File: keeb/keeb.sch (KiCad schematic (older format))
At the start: 156 parts, among them J1 AudioJack3, J101 USB_C_Receptacle_USB2.0, J102 AVR-ISP-6, SW101 SW_Push, SW102 SW_Push, SW103 SW_Push, SW104 SW_Push, SW105 SW_Push, SW106 SW_Push, SW107 SW_Push, SW108 SW_Push, SW109 SW_Push, SW110 SW_Push, SW111 SW_Push, SW112 SW_Push, SW113 SW_Push, SW114 SW_Push, SW115 SW_Push, SW116 SW_Push, SW117 SW_Push, SW118 SW_Push, SW119 SW_Push, SW120 SW_Push, SW121 SW_Push, SW122 SW_Push, SW123 SW_Push, SW124 SW_Push, SW125 SW_Push, SW126 SW_Push, SW127 SW_Push, SW128 SW_Push, SW129 SW_Push, SW130 SW_Push, SW131 SW_Push, SW132 SW_Push, SW133 SW_Push, SW134 SW_Push, SW135 SW_Push, SW136 SW_Push, SW137 SW_Push, SW138 SW_Push, SW139 SW_Push, SW140 SW_Push, SW141 SW_Push, SW142 SW_Push, SW143 SW_Push, SW144 SW_Push, SW145 SW_Push, SW146 SW_Push, SW147 SW_Push, SW148 SW_Push, SW149 SW_Push, SW150 SW_Push, SW151 SW_Push, SW152 SW_Push, SW153 SW_Push, SW154 SW_Push, SW155 SW_Push, SW156 SW_Push, SW157 SW_Push, SW158 SW_Push, SW159 SW_Push, SW160 SW_Push, SW161 SW_Push, SW162 SW_Push, SW163 SW_Push, SW164 SW_Push, SW165 SW_Push, SW166 SW_Push, SW167 SW_Push, U102 ATmega32U4-AU, Y1 16Mhz

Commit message: i2c fin
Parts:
- removed J1: AudioJack3, Connector_Audio:Jack_3.5mm_CUI_SJ-3523-SMT_Horizontal, symbol Connector:AudioJack3
- added J103, J104: AudioJack4, unORTHOdox_CF:Jack_3.5mm_TIC54-00177_Horizontal, symbol Connector:AudioJack4
- added R107, R108, R109, R110: 4K7, Resistor_SMD:R_0603_1608Metric_Pad0.98x0.95mm_HandSolder, symbol Device:R_Small
- J101: renamed from J102; man# (none) -> digi:839-54-00177CT-ND
- J102: renamed from J101; footprint Connector_USB:USB_C_Receptacle_Palconn_UTC16-G -> unORTHOdox_CF:USB_C_Receptacle_HRO_TYPE-C-31-M-12; man# (none) -> LCSC: C165948
- renumbered C109 to C106, C106 to C107, C107 to C108, C108 to C109, R105 to R101, R106 to R102, R101 to R103, R102 to R104, R103 to R105, R104 to R106, SW167 to SW101, SW101 to SW102, SW102 to SW103, SW103 to SW104, SW104 to SW105, SW105 to SW106, SW106 to SW107, SW107 to SW108, SW108 to SW109, SW109 to SW110, SW110 to SW111, SW111 to SW112, SW112 to SW113, SW113 to SW114, SW114 to SW115, SW115 to SW116, SW116 to SW117, SW117 to SW118, SW118 to SW119, SW119 to SW120, SW120 to SW121, SW121 to SW122, SW122 to SW123, SW123 to SW124, SW124 to SW125, SW125 to SW126, SW126 to SW127, SW127 to SW128, SW128 to SW129, SW129 to SW130, SW130 to SW131, SW131 to SW132, SW132 to SW133, SW133 to SW134, SW134 to SW135, SW135 to SW136, SW136 to SW137, SW137 to SW138, SW138 to SW139, SW139 to SW140, SW140 to SW141, SW141 to SW142, SW142 to SW143, SW143 to SW144, SW144 to SW145, SW145 to SW146, SW146 to SW147, SW147 to SW148, SW148 to SW149, SW149 to SW150, SW150 to SW151, SW151 to SW152, SW152 to SW153, SW153 to SW154, SW154 to SW155, SW155 to SW156, SW156 to SW157, SW157 to SW158, SW158 to SW159, SW159 to SW160, SW160 to SW161, SW161 to SW162, SW162 to SW163, SW163 to SW164, SW164 to SW165, SW165 to SW166, SW166 to SW167, U102 to U101, Y1 to Y101
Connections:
- net +5V: now also J103.S, J104.S, R107.1, R108.1, R109.1, R110.1
- net GND: now also J103.T, J104.T
- net SCL: now also J103.R1, J104.R1, R108.2, R110.2
- net SDA: now also J103.R2, J104.R2, R107.2, R109.2
- no-connect marks 6 -> 5

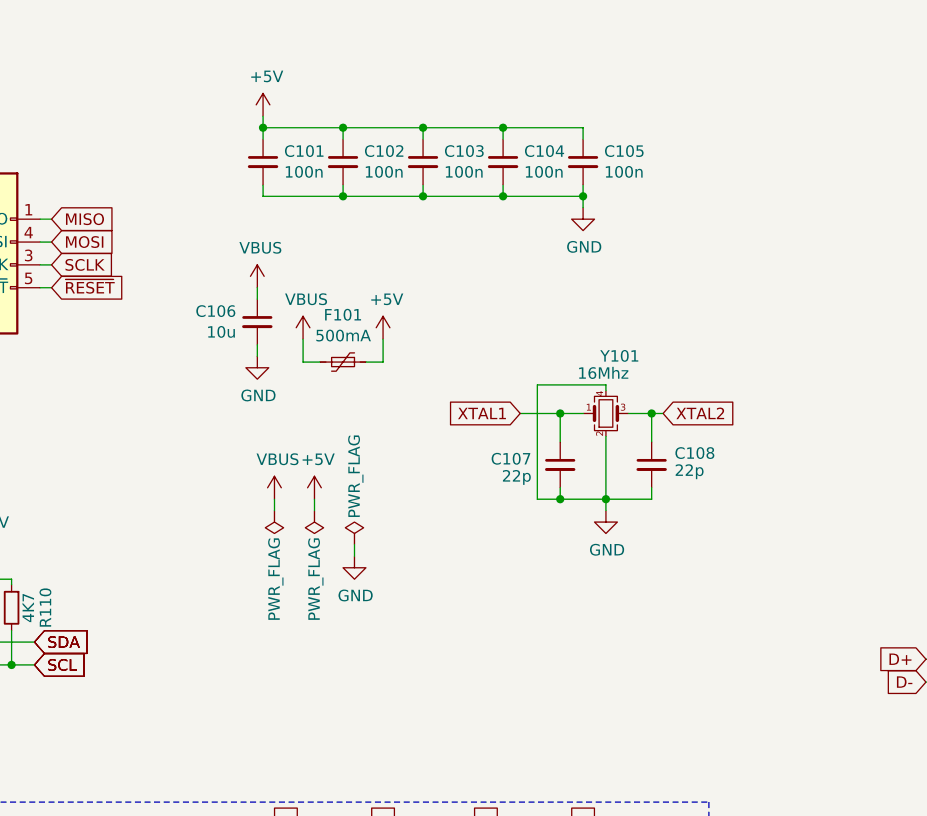
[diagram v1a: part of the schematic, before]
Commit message: updated bulk decoupling and usb-c routing
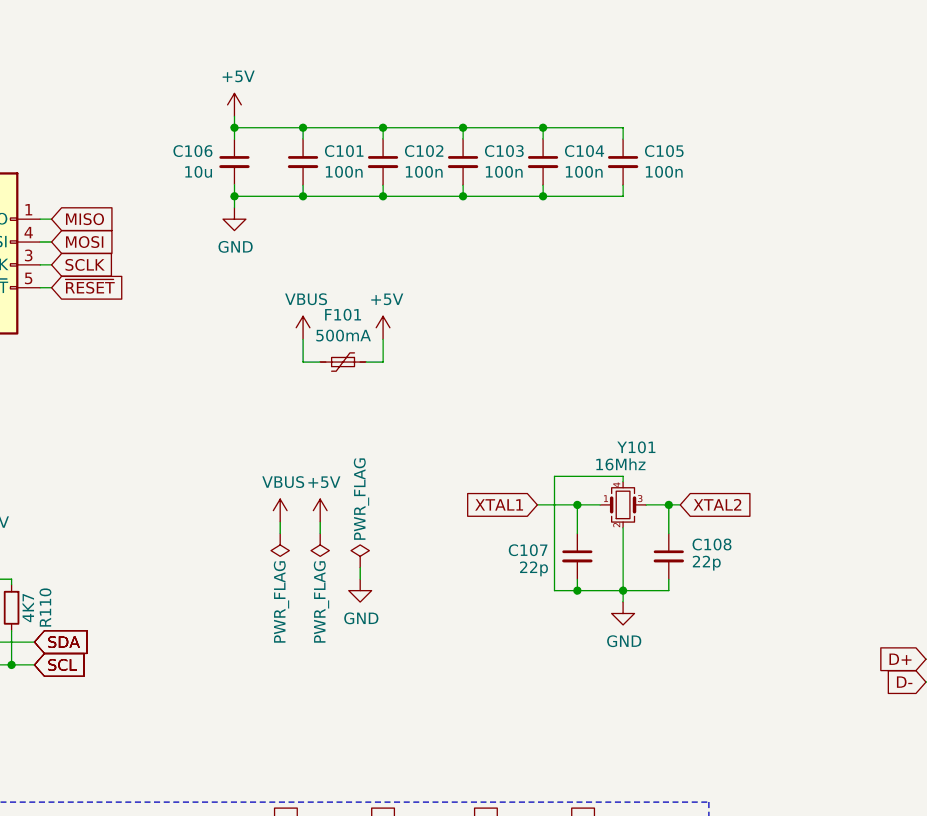
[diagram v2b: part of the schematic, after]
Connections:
- net +5V: now also C106.1
- net VBUS: no longer C106.1
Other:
- moved on the sheet: C101, C102, C103, C104, C105, C106, C107, C108, Y101

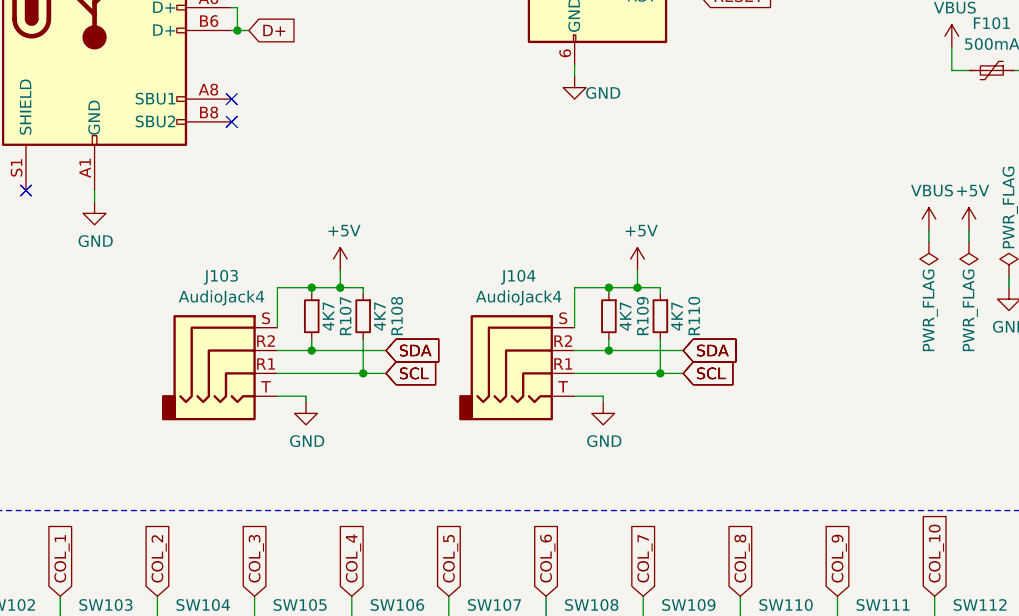
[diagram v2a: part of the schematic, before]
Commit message: fixed f mask fp
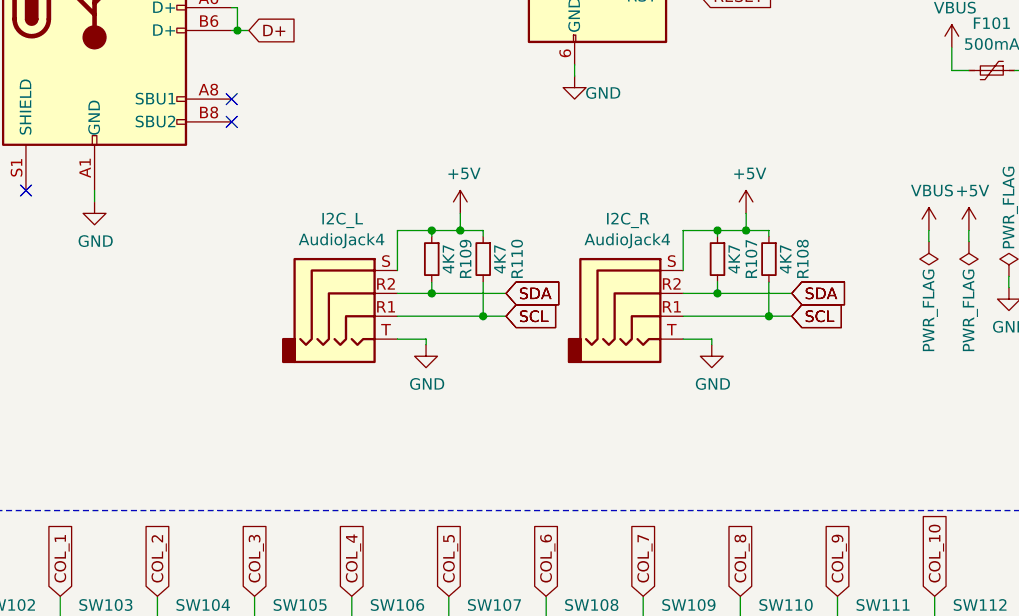
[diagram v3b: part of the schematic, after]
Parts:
- renumbered J104 to I2C_L, J103 to I2C_R
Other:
- moved on the sheet: I2C_L, I2C_R, R107, R108, R109, R110
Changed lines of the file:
@@
 $EndComp
 Wire Wire Line
-	2250 3650 2625 3650
-Wire Wire Line
-	2250 3550 2400 3550
-Text GLabel 2725 3650 2    50   Input ~ 0
-SCL
-Text GLabel 2725 3550 2    50   Input ~ 0
+	4025 3400 4400 3400
+Wire Wire Line
+	4025 3300 4175 3300
+Text GLabel 4500 3400 2    50   Input ~ 0
+SCL
+Text GLabel 4500 3300 2    50   Input ~ 0
 SDA
 $Comp
@@
 	-1   0    0    -1
 $EndComp
-Text GLabel 2725 3650 2    50   Input ~ 0
-SCL
-Text GLabel 2725 3550 2    50   Input ~ 0
-SDA
-$Comp
-L Connector:AudioJack4 J103
+Text GLabel 4500 3400 2    50   Input ~ 0
+SCL
+Text GLabel 4500 3300 2    50   Input ~ 0
+SDA
+$Comp
+L Connector:AudioJack4 I2C_R
 U 1 1 61BC1103
-P 2050 3550
-F 0 "J103" H 2007 3875 50  0000 C CNN
-F 1 "AudioJack4" H 2007 3784 50  0000 C CNN
-F 2 "unORTHOdox_CF:Jack_3.5mm_TIC54-00177_Horizontal" H 2050 3550 50  0001 C CNN
-F 3 "https://tensility.s3.amazonaws.com/uploads/pdffiles/54-00177.pdf?X-Amz-Expires=600&X-Amz-Date=20211128T005402Z&X-Amz-Algorithm=AWS4-HMAC-SHA256&X-Amz-Credential=AKIAIS2S4WRDQDSWDRZQ%2F20211128%2Fus-west-2%2Fs3%2Faws4_request&X-Amz-SignedHeaders=host&X-Amz-Signature=171e01fe49094ed0cdf1d5ee4dd310089a230a9be4a7cd19926a8270921837fa" H 2050 3550 50  0001 C CNN
-	1    2050 3550
+P 3825 3300
+F 0 "I2C_R" H 3782 3625 50  0000 C CNN
+F 1 "AudioJack4" H 3782 3534 50  0000 C CNN
+F 2 "unORTHOdox_CF:Jack_3.5mm_TIC54-00177_Horizontal" H 3825 3300 50  0001 C CNN
+F 3 "https://tensility.s3.amazonaws.com/uploads/pdffiles/54-00177.pdf?X-Amz-Expires=600&X-Amz-Date=20211128T005402Z&X-Amz-Algorithm=AWS4-HMAC-SHA256&X-Amz-Credential=AKIAIS2S4WRDQDSWDRZQ%2F20211128%2Fus-west-2%2Fs3%2Faws4_request&X-Amz-SignedHeaders=host&X-Amz-Signature=171e01fe49094ed0cdf1d5ee4dd310089a230a9be4a7cd19926a8270921837fa" H 3825 3300 50  0001 C CNN
+	1    3825 3300
 	1    0    0    -1
 $EndComp
@@
 L power:+5V #PWR0119
 U 1 1 61C73D46
-P 2525 3200
-F 0 "#PWR0119" H 2525 3050 50  0001 C CNN
-F 1 "+5V" H 2540 3373 50  0000 C CNN
-F 2 "" H 2525 3200 50  0001 C CNN
-F 3 "" H 2525 3200 50  0001 C CNN
-	1    2525 3200
+P 4300 2950
+F 0 "#PWR0119" H 4300 2800 50  0001 C CNN
+F 1 "+5V" H 4315 3123 50  0000 C CNN
+F 2 "" H 4300 2950 50  0001 C CNN
+F 3 "" H 4300 2950 50  0001 C CNN
+	1    4300 2950
 	1    0    0    -1
 $EndComp
@@
 L power:GND #PWR0122
 U 1 1 61CCF1E3
-P 2375 3775
-F 0 "#PWR0122" H 2375 3525 50  0001 C CNN
-F 1 "GND" H 2380 3602 50  0000 C CNN
-F 2 "" H 2375 3775 50  0001 C CNN
-F 3 "" H 2375 3775 50  0001 C CNN
-	1    2375 3775
-	1    0    0    -1
-$EndComp
-$Comp
-L Connector:AudioJack4 J104
+P 4150 3525
+F 0 "#PWR0122" H 4150 3275 50  0001 C CNN
+F 1 "GND" H 4155 3352 50  0000 C CNN
+F 2 "" H 4150 3525 50  0001 C CNN
+F 3 "" H 4150 3525 50  0001 C CNN
+	1    4150 3525
+	1    0    0    -1
+$EndComp
+$Comp
+L Connector:AudioJack4 I2C_L
 U 1 1 61CFCA38
-P 3350 3550
-F 0 "J104" H 3307 3875 50  0000 C CNN
-F 1 "AudioJack4" H 3307 3784 50  0000 C CNN
-F 2 "unORTHOdox_CF:Jack_3.5mm_TIC54-00177_Horizontal" H 3350 3550 50  0001 C CNN
-F 3 "https://tensility.s3.amazonaws.com/uploads/pdffiles/54-00177.pdf?X-Amz-Expires=600&X-Amz-Date=20211128T005402Z&X-Amz-Algorithm=AWS4-HMAC-SHA256&X-Amz-Credential=AKIAIS2S4WRDQDSWDRZQ%2F20211128%2Fus-west-2%2Fs3%2Faws4_request&X-Amz-SignedHeaders=host&X-Amz-Signature=171e01fe49094ed0cdf1d5ee4dd310089a230a9be4a7cd19926a8270921837fa" H 3350 3550 50  0001 C CNN
-	1    3350 3550
+P 2575 3300
+F 0 "I2C_L" H 2532 3625 50  0000 C CNN
+F 1 "AudioJack4" H 2532 3534 50  0000 C CNN
+F 2 "unORTHOdox_CF:Jack_3.5mm_TIC54-00177_Horizontal" H 2575 3300 50  0001 C CNN
+F 3 "https://tensility.s3.amazonaws.com/uploads/pdffiles/54-00177.pdf?X-Amz-Expires=600&X-Amz-Date=20211128T005402Z&X-Amz-Algorithm=AWS4-HMAC-SHA256&X-Amz-Credential=AKIAIS2S4WRDQDSWDRZQ%2F20211128%2Fus-west-2%2Fs3%2Faws4_request&X-Amz-SignedHeaders=host&X-Amz-Signature=171e01fe49094ed0cdf1d5ee4dd310089a230a9be4a7cd19926a8270921837fa" H 2575 3300 50  0001 C CNN
+	1    2575 3300
 	1    0    0    -1
 $EndComp
@@
 L Device:R_Small R107
 U 1 1 61EAFBF0
-P 2400 3400
-F 0 "R107" V 2250 3400 50  0000 C CNN
-F 1 "4K7" V 2325 3400 50  0000 C CNN
-F 2 "Resistor_SMD:R_0603_1608Metric_Pad0.98x0.95mm_HandSolder" H 2400 3400 50  0001 C CNN
-F 3 "~" H 2400 3400 50  0001 C CNN
-	1    2400 3400
+P 4175 3150
+F 0 "R107" V 4025 3150 50  0000 C CNN
+F 1 "4K7" V 4100 3150 50  0000 C CNN
+F 2 "Resistor_SMD:R_0603_1608Metric_Pad0.98x0.95mm_HandSolder" H 4175 3150 50  0001 C CNN
+F 3 "~" H 4175 3150 50  0001 C CNN
+	1    4175 3150
 	-1   0    0    -1
 $EndComp
@@
 L Device:R_Small R108
 U 1 1 61EB0A1A
-P 2625 3400
-F 0 "R108" V 2475 3400 50  0000 C CNN
-F 1 "4K7" V 2550 3400 50  0000 C CNN
-F 2 "Resistor_SMD:R_0603_1608Metric_Pad0.98x0.95mm_HandSolder" H 2625 3400 50  0001 C CNN
-F 3 "~" H 2625 3400 50  0001 C CNN
-	1    2625 3400
-	-1   0    0    -1
-$EndComp
-Wire Wire Line
-	2400 3500 2400 3550
-Connection ~ 2400 3550
-Wire Wire Line
-	2400 3550 2725 3550
-Wire Wire Line
-	2625 3500 2625 3650
-Connection ~ 2625 3650
-Wire Wire Line
-	2625 3650 2725 3650
-Wire Wire Line
-	2625 3300 2625 3275
-Wire Wire Line
-	2625 3275 2525 3275
-Wire Wire Line
-	2400 3275 2400 3300
-Wire Wire Line
-	2250 3275 2250 3450
-Wire Wire Line
-	2250 3275 2400 3275
-Connection ~ 2400 3275
-Wire Wire Line
-	2525 3200 2525 3275
-Connection ~ 2525 3275
-Wire Wire Line
-	2525 3275 2400 3275
-Wire Wire Line
-	2250 3750 2375 3750
-Wire Wire Line
-	2375 3750 2375 3775
-Wire Wire Line
-	3550 3650 3925 3650
-Wire Wire Line
-	3550 3550 3700 3550
-Text GLabel 4025 3650 2    50   Input ~ 0
-SCL
-Text GLabel 4025 3550 2    50   Input ~ 0
-SDA
-Text GLabel 4025 3650 2    50   Input ~ 0
-SCL
-Text GLabel 4025 3550 2    50   Input ~ 0
+P 4400 3150
+F 0 "R108" V 4250 3150 50  0000 C CNN
+F 1 "4K7" V 4325 3150 50  0000 C CNN
+F 2 "Resistor_SMD:R_0603_1608Metric_Pad0.98x0.95mm_HandSolder" H 4400 3150 50  0001 C CNN
+F 3 "~" H 4400 3150 50  0001 C CNN
+	1    4400 3150
+	-1   0    0    -1
+$EndComp
+Wire Wire Line
+	4175 3250 4175 3300
+Connection ~ 4175 3300
+Wire Wire Line
+	4175 3300 4500 3300
+Wire Wire Line
+	4400 3250 4400 3400
+Connection ~ 4400 3400
+Wire Wire Line
+	4400 3400 4500 3400
+Wire Wire Line
+	4400 3050 4400 3025
+Wire Wire Line
+	4400 3025 4300 3025
+Wire Wire Line
+	4175 3025 4175 3050
+Wire Wire Line
+	4025 3025 4025 3200
+Wire Wire Line
+	4025 3025 4175 3025
+Connection ~ 4175 3025
+Wire Wire Line
+	4300 2950 4300 3025
+Connection ~ 4300 3025
+Wire Wire Line
+	4300 3025 4175 3025
+Wire Wire Line
+	4025 3500 4150 3500
+Wire Wire Line
+	4150 3500 4150 3525
+Wire Wire Line
+	2775 3400 3150 3400
+Wire Wire Line
+	2775 3300 2925 3300
+Text GLabel 3250 3400 2    50   Input ~ 0
+SCL
+Text GLabel 3250 3300 2    50   Input ~ 0
+SDA
+Text GLabel 3250 3400 2    50   Input ~ 0
+SCL
+Text GLabel 3250 3300 2    50   Input ~ 0
 SDA
 $Comp
 L power:+5V #PWR0120
 U 1 1 6212A42A
-P 3825 3200
-F 0 "#PWR0120" H 3825 3050 50  0001 C CNN
-F 1 "+5V" H 3840 3373 50  0000 C CNN
-F 2 "" H 3825 3200 50  0001 C CNN
-F 3 "" H 3825 3200 50  0001 C CNN
-	1    3825 3200
+P 3050 2950
+F 0 "#PWR0120" H 3050 2800 50  0001 C CNN
+F 1 "+5V" H 3065 3123 50  0000 C CNN
+F 2 "" H 3050 2950 50  0001 C CNN
+F 3 "" H 3050 2950 50  0001 C CNN
+	1    3050 2950
 	1    0    0    -1
 $EndComp
@@
 L power:GND #PWR0123
 U 1 1 6212A434
-P 3675 3775
-F 0 "#PWR0123" H 3675 3525 50  0001 C CNN
-F 1 "GND" H 3680 3602 50  0000 C CNN
-F 2 "" H 3675 3775 50  0001 C CNN
-F 3 "" H 3675 3775 50  0001 C CNN
-	1    3675 3775
+P 2900 3525
+F 0 "#PWR0123" H 2900 3275 50  0001 C CNN
+F 1 "GND" H 2905 3352 50  0000 C CNN
+F 2 "" H 2900 3525 50  0001 C CNN
+F 3 "" H 2900 3525 50  0001 C CNN
+	1    2900 3525
 	1    0    0    -1
 $EndComp
@@
 L Device:R_Small R109
 U 1 1 6212A43E
-P 3700 3400
-F 0 "R109" V 3550 3400 50  0000 C CNN
-F 1 "4K7" V 3625 3400 50  0000 C CNN
-F 2 "Resistor_SMD:R_0603_1608Metric_Pad0.98x0.95mm_HandSolder" H 3700 3400 50  0001 C CNN
-F 3 "~" H 3700 3400 50  0001 C CNN
-	1    3700 3400
+P 2925 3150
+F 0 "R109" V 2775 3150 50  0000 C CNN
+F 1 "4K7" V 2850 3150 50  0000 C CNN
+F 2 "Resistor_SMD:R_0603_1608Metric_Pad0.98x0.95mm_HandSolder" H 2925 3150 50  0001 C CNN
+F 3 "~" H 2925 3150 50  0001 C CNN
+	1    2925 3150
 	-1   0    0    -1
 $EndComp
@@
 L Device:R_Small R110
 U 1 1 6212A448
-P 3925 3400
-F 0 "R110" V 3775 3400 50  0000 C CNN
-F 1 "4K7" V 3850 3400 50  0000 C CNN
-F 2 "Resistor_SMD:R_0603_1608Metric_Pad0.98x0.95mm_HandSolder" H 3925 3400 50  0001 C CNN
-F 3 "~" H 3925 3400 50  0001 C CNN
-	1    3925 3400
-	-1   0    0    -1
-$EndComp
-Wire Wire Line
-	3700 3500 3700 3550
-Connection ~ 3700 3550
-Wire Wire Line
-	3700 3550 4025 3550
-Wire Wire Line
-	3925 3500 3925 3650
-Connection ~ 3925 3650
-Wire Wire Line
-	3925 3650 4025 3650
-Wire Wire Line
-	3925 3300 3925 3275
-Wire Wire Line
-	3925 3275 3825 3275
-Wire Wire Line
-	3700 3275 3700 3300
-Wire Wire Line
-	3550 3275 3700 3275
-Connection ~ 3700 3275
-Wire Wire Line
-	3825 3200 3825 3275
-Connection ~ 3825 3275
-Wire Wire Line
-	3825 3275 3700 3275
-Wire Wire Line
-	3550 3750 3675 3750
-Wire Wire Line
-	3675 3750 3675 3775
-Wire Wire Line
-	3550 3275 3550 3450
+P 3150 3150
+F 0 "R110" V 3000 3150 50  0000 C CNN
+F 1 "4K7" V 3075 3150 50  0000 C CNN
+F 2 "Resistor_SMD:R_0603_1608Metric_Pad0.98x0.95mm_HandSolder" H 3150 3150 50  0001 C CNN
+F 3 "~" H 3150 3150 50  0001 C CNN
+	1    3150 3150
+	-1   0    0    -1
+$EndComp
+Wire Wire Line
+	2925 3250 2925 3300
+Connection ~ 2925 3300
+Wire Wire Line
+	2925 3300 3250 3300
+Wire Wire Line
+	3150 3250 3150 3400
+Connection ~ 3150 3400
+Wire Wire Line
+	3150 3400 3250 3400
+Wire Wire Line
+	3150 3050 3150 3025
+Wire Wire Line
+	3150 3025 3050 3025
+Wire Wire Line
+	2925 3025 2925 3050
+Wire Wire Line
+	2775 3025 2925 3025
+Connection ~ 2925 3025
+Wire Wire Line
+	3050 2950 3050 3025
+Connection ~ 3050 3025
+Wire Wire Line
+	3050 3025 2925 3025
+Wire Wire Line
+	2775 3500 2900 3500
+Wire Wire Line
+	2900 3500 2900 3525
+Wire Wire Line
+	2775 3025 2775 3200
 Wire Wire Line
 	5200 1600 4900 1600

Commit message: silk cleanu
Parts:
- renumbered I2C_L to I2C_101, I2C_R to I2C_102
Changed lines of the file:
@@
 SDA
 $Comp
-L Connector:AudioJack4 I2C_R
+L Connector:AudioJack4 I2C_102
 U 1 1 61BC1103
 P 3825 3300
-F 0 "I2C_R" H 3782 3625 50  0000 C CNN
+F 0 "I2C_102" H 3782 3625 50  0000 C CNN
 F 1 "AudioJack4" H 3782 3534 50  0000 C CNN
 F 2 "unORTHOdox_CF:Jack_3.5mm_TIC54-00177_Horizontal" H 3825 3300 50  0001 C CNN
@@
 $EndComp
 $Comp
-L Connector:AudioJack4 I2C_L
+L Connector:AudioJack4 I2C_101
 U 1 1 61CFCA38
 P 2575 3300
-F 0 "I2C_L" H 2532 3625 50  0000 C CNN
+F 0 "I2C_101" H 2532 3625 50  0000 C CNN
 F 1 "AudioJack4" H 2532 3534 50  0000 C CNN
 F 2 "unORTHOdox_CF:Jack_3.5mm_TIC54-00177_Horizontal" H 2575 3300 50  0001 C CNN
